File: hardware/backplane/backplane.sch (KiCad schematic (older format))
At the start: 88 parts, among them J1 C96ABC, J10 Conn_Coaxial_Power, J2 C96ABC, J3 C96ABC, J4 C96ABC, J5 C96ABC, J6 C96ABC, J7 C96ABC, J8 C96ABC, J9 C96ABC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

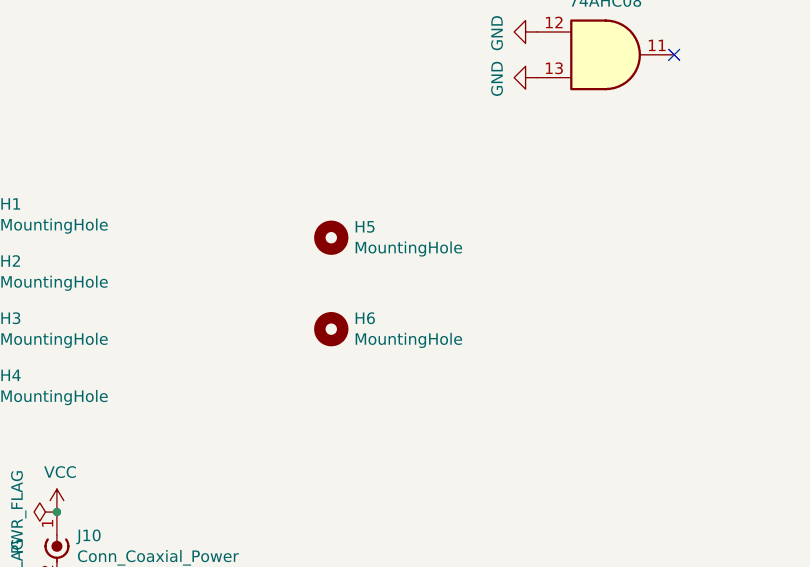
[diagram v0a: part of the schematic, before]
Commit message: backplane: reduce mounting hardware used
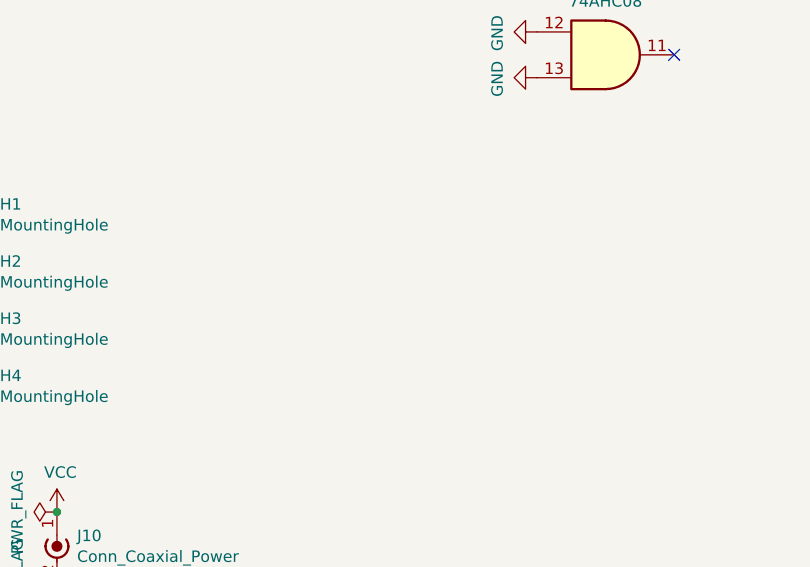
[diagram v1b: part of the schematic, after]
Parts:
- removed H5, H6: MountingHole, rails:7mm, symbol Mechanical:MountingHole
- H1, H2, H3, H4: footprint rails:8mm -> rails:m5-close
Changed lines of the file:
@@
 F 0 "H4" H 12250 5546 50  0000 L CNN
 F 1 "MountingHole" H 12250 5455 50  0000 L CNN
-F 2 "rails:8mm" H 12150 5500 50  0001 C CNN
+F 2 "rails:m5-close" H 12150 5500 50  0001 C CNN
 F 3 "~" H 12150 5500 50  0001 C CNN
 	1    12150 5500
@@
 F 0 "H3" H 12250 5296 50  0000 L CNN
 F 1 "MountingHole" H 12250 5205 50  0000 L CNN
-F 2 "rails:8mm" H 12150 5250 50  0001 C CNN
+F 2 "rails:m5-close" H 12150 5250 50  0001 C CNN
 F 3 "~" H 12150 5250 50  0001 C CNN
 	1    12150 5250
@@
 F 0 "H2" H 12250 5046 50  0000 L CNN
 F 1 "MountingHole" H 12250 4955 50  0000 L CNN
-F 2 "rails:8mm" H 12150 5000 50  0001 C CNN
+F 2 "rails:m5-close" H 12150 5000 50  0001 C CNN
 F 3 "~" H 12150 5000 50  0001 C CNN
 	1    12150 5000
@@
 F 0 "H1" H 12250 4796 50  0000 L CNN
 F 1 "MountingHole" H 12250 4705 50  0000 L CNN
-F 2 "rails:8mm" H 12150 4750 50  0001 C CNN
+F 2 "rails:m5-close" H 12150 4750 50  0001 C CNN
 F 3 "~" H 12150 4750 50  0001 C CNN
 	1    12150 4750
@@
 	-650 -2650 -700 -2650
 $Comp
-L Mechanical:MountingHole H5
-U 1 1 A242A775
-P 13700 4850
-F 0 "H5" H 13800 4896 50  0000 L CNN
-F 1 "MountingHole" H 13800 4805 50  0000 L CNN
-F 2 "rails:7mm" H 13700 4850 50  0001 C CNN
-F 3 "~" H 13700 4850 50  0001 C CNN
-	1    13700 4850
-	1    0    0    -1
-$EndComp
-$Comp
-L Mechanical:MountingHole H6
-U 1 1 A2589AFB
-P 13700 5250
-F 0 "H6" H 13800 5296 50  0000 L CNN
-F 1 "MountingHole" H 13800 5205 50  0000 L CNN
-F 2 "rails:7mm" H 13700 5250 50  0001 C CNN
-F 3 "~" H 13700 5250 50  0001 C CNN
-	1    13700 5250
-	1    0    0    -1
-$EndComp
-$Comp
 L Device:D_Schottky_x2_KCom_AAK D3

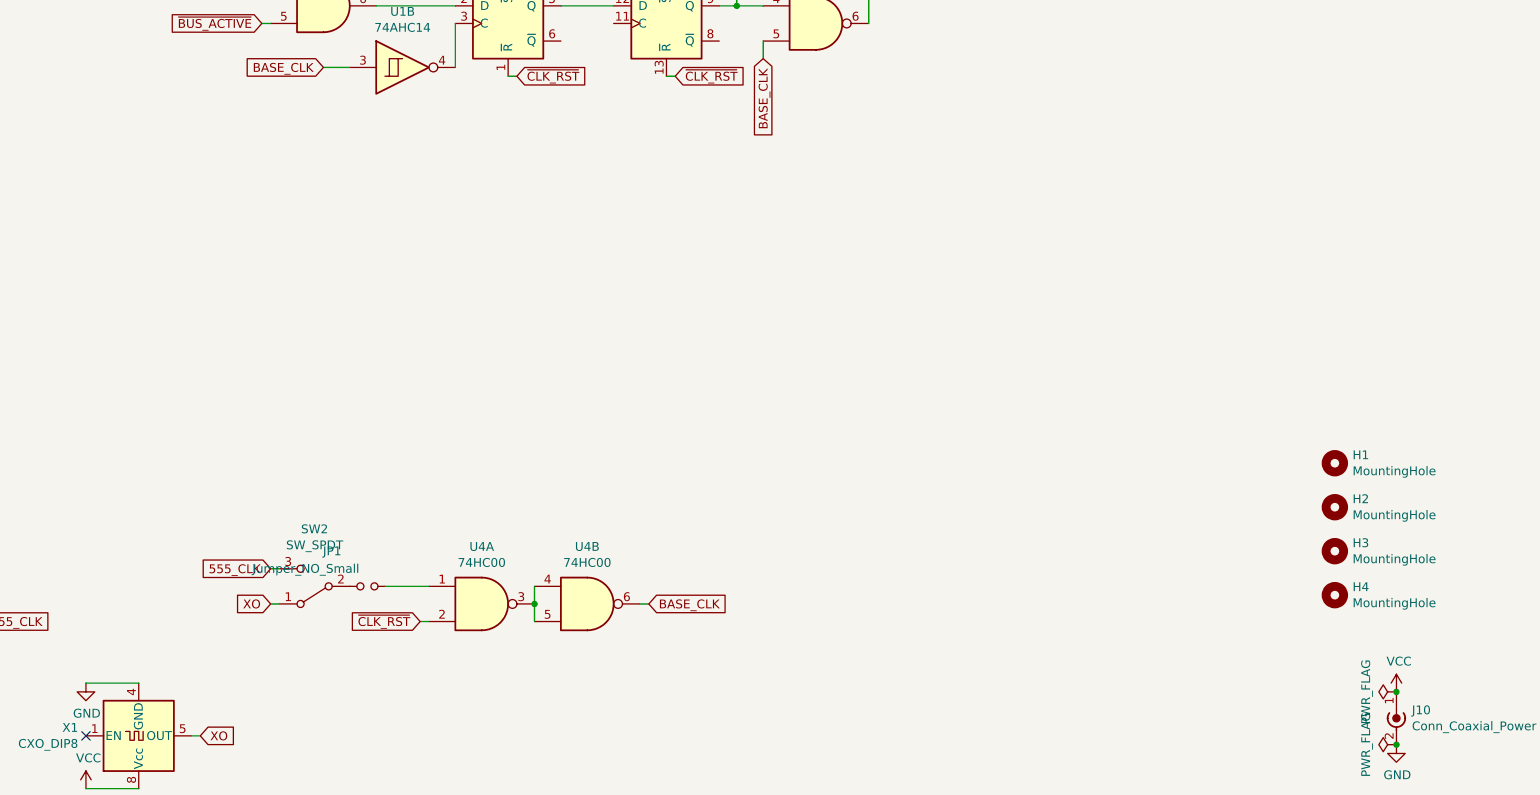
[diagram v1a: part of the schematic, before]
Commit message: backplane: add soft power on/off circuit to backplane
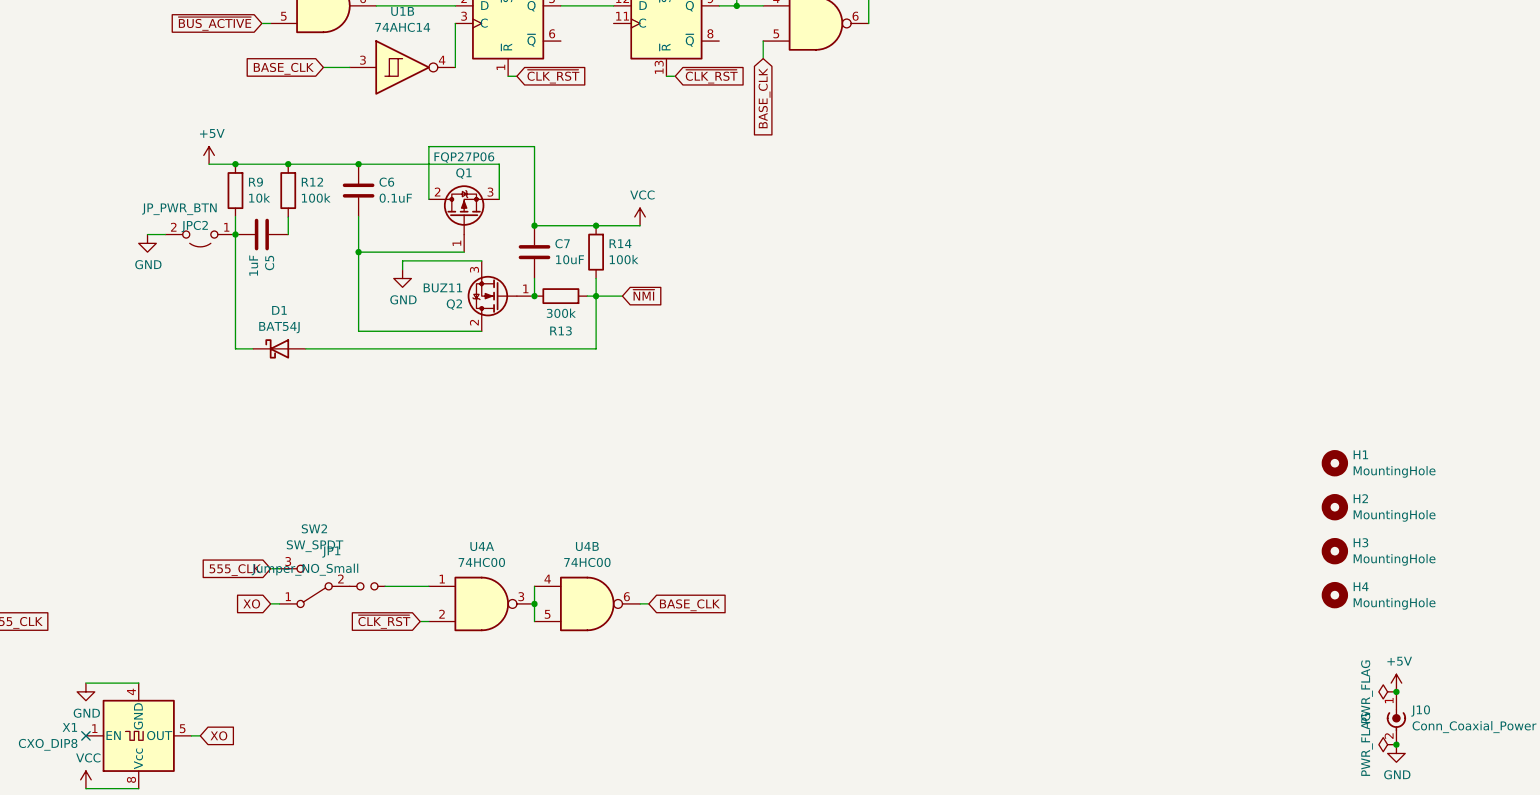
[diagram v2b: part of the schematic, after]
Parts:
- added C5: 1uF, Capacitor_THT:C_Axial_L5.1mm_D3.1mm_P7.50mm_Horizontal, symbol Device:C
- added C6: 0.1uF, Capacitor_THT:C_Disc_D4.7mm_W2.5mm_P5.00mm, symbol Device:C
- added C7: 10uF, Capacitor_THT:C_Axial_L5.1mm_D3.1mm_P7.50mm_Horizontal, symbol Device:C
- added D1: BAT54J, Diode_THT:D_A-405_P7.62mm_Horizontal, symbol Diode:BAT54J
- added JPC2: JP_PWR_BTN, Connector_PinHeader_2.54mm:PinHeader_1x02_P2.54mm_Vertical, symbol Jumper:Jumper_2_Open
- added Q1: FQP27P06, Package_TO_SOT_THT:TO-220-3_Horizontal_TabDown, symbol Transistor_FET:FQP27P06
- added Q2: BUZ11, Package_TO_SOT_THT:TO-220-3_Horizontal_TabDown, symbol Transistor_FET:BUZ11
- added R12, R14: 100k, Resistor_THT:R_Axial_DIN0207_L6.3mm_D2.5mm_P7.62mm_Horizontal, symbol Device:R
- added R13: 300k, Resistor_THT:R_Axial_DIN0207_L6.3mm_D2.5mm_P7.62mm_Horizontal, symbol Device:R
- added R9: 10k, Resistor_THT:R_Axial_DIN0207_L6.3mm_D2.5mm_P7.62mm_Horizontal, symbol Device:R
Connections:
- net A30: now also D1.2 (A), R13.2, R14.1
- net GND: now also JPC2.2 (B), Q2.3 (S)
- net VCC: now also C7.1, Q1.2 (D), R14.2; no longer J10.1 (In)
- new net: C6.2, Q1.1 (G), Q2.2 (D)
- new net: C7.2, Q2.1 (G), R13.1
- new net: C5.2, D1.1 (K), JPC2.1 (A), R9.1
- new net: C5.1, R12.1
- new net +5V: C6.1, J10.1 (In), Q1.3 (S), R12.2, R9.2
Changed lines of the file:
@@
 $EndDescr
 $Comp
-L power:VCC #PWR055
-U 1 1 60477C9A
-P 12500 6050
-F 0 "#PWR055" H 12500 5900 50  0001 C CNN
-F 1 "VCC" H 12515 6223 50  0000 C CNN
-F 2 "" H 12500 6050 50  0001 C CNN
-F 3 "" H 12500 6050 50  0001 C CNN
-	1    12500 6050
-	1    0    0    -1
-$EndComp
-$Comp
 L power:GND #PWR056
 U 1 1 60478083
@@
 $EndComp
 Connection ~ 12500 6350
-Connection ~ 12500 6050
 $Comp
 L Connector:TestPoint TP1
@@
 	1    0    0    -1
 $EndComp
+$Comp
+L Transistor_FET:BUZ11 Q2
+U 1 1 610FD02B
+P 7400 3800
+F 0 "Q2" H 7605 3846 50  0000 L CNN
+F 1 "BUZ11" H 7605 3755 50  0000 L CNN
+F 2 "Package_TO_SOT_THT:TO-220-3_Horizontal_TabDown" H 7650 3725 50  0001 L CIN
+F 3 "https://media.digikey.com/pdf/Data%20Sheets/Fairchild%20PDFs/BUZ11.pdf" H 7400 3800 50  0001 L CNN
+	1    7400 3800
+	-1   0    0    1
+$EndComp
+$Comp
+L power:GND #PWR0103
+U 1 1 61589CAB
+P 6850 3650
+F 0 "#PWR0103" H 6850 3400 50  0001 C CNN
+F 1 "GND" H 6855 3477 50  0000 C CNN
+F 2 "" H 6850 3650 50  0001 C CNN
+F 3 "" H 6850 3650 50  0001 C CNN
+	1    6850 3650
+	1    0    0    -1
+$EndComp
+Wire Wire Line
+	6850 3650 6850 3600
+Wire Wire Line
+	6850 3600 7300 3600
+$Comp
+L Device:R R13
+U 1 1 61710642
+P 7750 3800
+F 0 "R13" V 7550 3800 50  0000 C CNN
+F 1 "300k" V 7650 3800 50  0000 C CNN
+F 2 "Resistor_THT:R_Axial_DIN0207_L6.3mm_D2.5mm_P7.62mm_Horizontal" V 7680 3800 50  0001 C CNN
+F 3 "~" H 7750 3800 50  0001 C CNN
+	1    7750 3800
+	0    -1   -1   0
+$EndComp
+$Comp
+L Device:R R14
+U 1 1 61899D83
+P 7950 3550
+F 0 "R14" H 7880 3504 50  0000 R CNN
+F 1 "100k" H 7880 3595 50  0000 R CNN
+F 2 "Resistor_THT:R_Axial_DIN0207_L6.3mm_D2.5mm_P7.62mm_Horizontal" V 7880 3550 50  0001 C CNN
+F 3 "~" H 7950 3550 50  0001 C CNN
+	1    7950 3550
+	-1   0    0    1
+$EndComp
+Wire Wire Line
+	7950 3700 7950 3800
+$Comp
+L Device:C C7
+U 1 1 61A1E32F
+P 7600 3550
+F 0 "C7" H 7715 3596 50  0000 L CNN
+F 1 "10uF" H 7715 3505 50  0000 L CNN
+F 2 "Capacitor_THT:C_Axial_L5.1mm_D3.1mm_P7.50mm_Horizontal" H 7638 3400 50  0001 C CNN
+F 3 "~" H 7600 3550 50  0001 C CNN
+	1    7600 3550
+	1    0    0    -1
+$EndComp
+Wire Wire Line
+	7600 3800 7600 3700
+Wire Wire Line
+	7950 3800 7900 3800
+Wire Wire Line
+	7600 3400 7950 3400
+Connection ~ 7600 3400
+$Comp
+L power:+5V #PWR0108
+U 1 1 6295B29C
+P 12500 6050
+F 0 "#PWR0108" H 12500 5900 50  0001 C CNN
+F 1 "+5V" H 12515 6223 50  0000 C CNN
+F 2 "" H 12500 6050 50  0001 C CNN
+F 3 "" H 12500 6050 50  0001 C CNN
+	1    12500 6050
+	1    0    0    -1
+$EndComp
+Connection ~ 12500 6050
+$Comp
+L power:VCC #PWR055
+U 1 1 60477C9A
+P 8200 3400
+F 0 "#PWR055" H 8200 3250 50  0001 C CNN
+F 1 "VCC" H 8215 3573 50  0000 C CNN
+F 2 "" H 8200 3400 50  0001 C CNN
+F 3 "" H 8200 3400 50  0001 C CNN
+	1    8200 3400
+	1    0    0    -1
+$EndComp
+Wire Wire Line
+	7950 3400 8200 3400
+Connection ~ 7950 3400
+$Comp
+L power:+5V #PWR0109
+U 1 1 63284480
+P 5750 3050
+F 0 "#PWR0109" H 5750 2900 50  0001 C CNN
+F 1 "+5V" H 5765 3223 50  0000 C CNN
+F 2 "" H 5750 3050 50  0001 C CNN
+F 3 "" H 5750 3050 50  0001 C CNN
+	1    5750 3050
+	1    0    0    -1
+$EndComp
+Wire Wire Line
+	5750 3050 5900 3050
+$Comp
+L Device:R R9
+U 1 1 635960F7
+P 5900 3200
+F 0 "R9" H 5830 3154 50  0000 R CNN
+F 1 "10k" H 5830 3245 50  0000 R CNN
+F 2 "Resistor_THT:R_Axial_DIN0207_L6.3mm_D2.5mm_P7.62mm_Horizontal" V 5830 3200 50  0001 C CNN
+F 3 "~" H 5900 3200 50  0001 C CNN
+	1    5900 3200
+	-1   0    0    1
+$EndComp
+Connection ~ 5900 3050
+Wire Wire Line
+	5900 3050 6200 3050
+$Comp
+L Device:R R12
+U 1 1 6359666D
+P 6200 3200
+F 0 "R12" H 6130 3154 50  0000 R CNN
+F 1 "100k" H 6130 3245 50  0000 R CNN
+F 2 "Resistor_THT:R_Axial_DIN0207_L6.3mm_D2.5mm_P7.62mm_Horizontal" V 6130 3200 50  0001 C CNN
+F 3 "~" H 6200 3200 50  0001 C CNN
+	1    6200 3200
+	-1   0    0    1
+$EndComp
+Connection ~ 6200 3050
+Wire Wire Line
+	6200 3050 6600 3050
+$Comp
+L Device:C C6
+U 1 1 6359692F
+P 6600 3200
+F 0 "C6" H 6715 3246 50  0000 L CNN
+F 1 "0.1uF" H 6715 3155 50  0000 L CNN
+F 2 "Capacitor_THT:C_Disc_D4.7mm_W2.5mm_P5.00mm" H 6638 3050 50  0001 C CNN
+F 3 "~" H 6600 3200 50  0001 C CNN
+	1    6600 3200
+	1    0    0    -1
+$EndComp
+Connection ~ 6600 3050
+$Comp
+L Transistor_FET:FQP27P06 Q1
+U 1 1 60AF6494
+P 7200 3350
+F 0 "Q1" V 7449 3350 50  0000 C CNN
+F 1 "FQP27P06" V 7540 3350 50  0000 C CNN
+F 2 "Package_TO_SOT_THT:TO-220-3_Horizontal_TabDown" H 7400 3275 50  0001 L CIN
+F 3 "https://www.onsemi.com/pub/Collateral/FQP27P06-D.PDF" H 7200 3350 50  0001 L CNN
+	1    7200 3350
+	0    -1   -1   0
+$EndComp
+Wire Wire Line
+	7400 3050 7400 3250
+Wire Wire Line
+	6600 3050 7400 3050
+Wire Wire Line
+	7000 3250 7000 2950
+Wire Wire Line
+	7000 2950 7600 2950
+Wire Wire Line
+	7600 2950 7600 3400
+Wire Wire Line
+	6200 3350 6200 3450
+Wire Wire Line
+	5900 3350 5900 3450
+$Comp
+L Device:C C5
+U 1 1 63D536BB
+P 6050 3450
+F 0 "C5" H 6165 3496 50  0000 L CNN
+F 1 "1uF" H 6165 3405 50  0000 L CNN
+F 2 "Capacitor_THT:C_Axial_L5.1mm_D3.1mm_P7.50mm_Horizontal" H 6088 3300 50  0001 C CNN
+F 3 "~" H 6050 3450 50  0001 C CNN
+	1    6050 3450
+	0    1    1    0
+$EndComp
+Wire Wire Line
+	6600 4000 6600 3550
+Wire Wire Line
+	7200 3550 6600 3550
+Connection ~ 6600 3550
+Wire Wire Line
+	6600 3550 6600 3350
+Wire Wire Line
+	7300 4000 6600 4000
+Connection ~ 7600 3800
+$Comp
+L Diode:BAT54J D1
+U 1 1 6549C471
+P 6150 4100
+F 0 "D1" H 6150 4317 50  0000 C CNN
+F 1 "BAT54J" H 6150 4226 50  0000 C CNN
+F 2 "Diode_THT:D_A-405_P7.62mm_Horizontal" H 6150 3925 50  0001 C CNN
+F 3 "https://assets.nexperia.com/documents/data-sheet/BAT54J.pdf" H 6150 4100 50  0001 C CNN
+	1    6150 4100
+	1    0    0    -1
+$EndComp
+Wire Wire Line
+	7950 3800 7950 4100
+Wire Wire Line
+	7950 4100 6300 4100
+Connection ~ 7950 3800
+Wire Wire Line
+	6000 4100 5900 4100
+Wire Wire Line
+	5900 4100 5900 3450
+Connection ~ 5900 3450
+$Comp
+L Jumper:Jumper_2_Open JPC2
+U 1 1 65ADC663
+P 5700 3450
+F 0 "JPC2" H 5650 3400 50  0000 L CNN
+F 1 "JP_PWR_BTN" H 5600 3300 50  0000 L CNN
+F 2 "Connector_PinHeader_2.54mm:PinHeader_1x02_P2.54mm_Vertical" H 5700 3450 50  0001 C CNN
+F 3 "~" H 5700 3450 50  0001 C CNN
+	1    5700 3450
+	-1   0    0    1
+$EndComp
+$Comp
+L power:GND #gnd0115
+U 1 1 65ADD10B
+P 5400 3450
+F 0 "#gnd0115" H 5400 3200 50  0001 C CNN
+F 1 "GND" H 5405 3277 50  0000 C CNN
+F 2 "" H 5400 3450 50  0001 C CNN
+F 3 "" H 5400 3450 50  0001 C CNN
+	1    5400 3450
+	1    0    0    -1
+$EndComp
+Wire Wire Line
+	5500 3450 5400 3450
+Text GLabel 8100 3800 2    50   Input ~ 0
+~NMI~
+Wire Wire Line
+	8100 3800 7950 3800
 $EndSCHEMATC

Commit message: backplane: minor improvements
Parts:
- removed D3: D_Schottky_x2_KCom_AAK, Package_TO_SOT_SMD:SOT-23_Handsoldering, symbol Device:D_Schottky_x2_KCom_AAK
- added C8: CP, Capacitor_THT:CP_Radial_D10.0mm_P5.00mm, symbol Device:CP
- added D2, D4: LED, LED_THT:LED_D3.0mm, symbol Device:LED
- added D3, D5: BAT54J, Diode_THT:D_A-405_P7.62mm_Horizontal, symbol Diode:BAT54J
- added R15, R16: 1k, Resistor_THT:R_Axial_DIN0207_L6.3mm_D2.5mm_P7.62mm_Horizontal, symbol Device:R
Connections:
- net +5V: now also C8.1, D4.2 (A)
- net GND: now also C8.2, R15.1, R16.1
- net VCC: now also D2.2 (A)
- net ~RST_HDR~: now also D3.1 (K), D5.1 (K)
- net at CR1.1, R2.2, U1.5: now also D3.2 (A)
- net at CR2.1, R3.2, U1.13: now also D5.2 (A)
- new net: D2.1 (K), R15.2
- new net: D4.1 (K), R16.2
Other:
- moved on the sheet: C5, C6, C7, CBU1, CBU10, CBU2, CBU3, CBU4, CBU5, CBU6, CBU7, CBU8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

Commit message: start adding reverse voltage protection
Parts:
- removed JPC1: JP_RST, Connector_PinHeader_2.54mm:PinHeader_1x02_P2.54mm_Vertical, symbol Jumper:Jumper_2_Open
- removed JPC2: JP_PWR_BTN, Connector_PinHeader_2.54mm:PinHeader_1x02_P2.54mm_Vertical, symbol Jumper:Jumper_2_Open
- added D?: D_Zener, Diode_THT:D_A-405_P7.62mm_Horizontal, symbol Device:D_Zener
- added F?: Fuse, symbol Device:Fuse
- added Q?: FQP27P06, Package_TO_SOT_THT:TO-220-3_Horizontal_TabDown, symbol Transistor_FET:FQP27P06
- added R?: 100k, Resistor_THT:R_Axial_DIN0207_L6.3mm_D2.5mm_P7.62mm_Horizontal, symbol Device:R
- added SW4, SW5: SW_Push, Connector_PinHeader_2.54mm:PinHeader_1x02_P2.54mm_Vertical, symbol Switch:SW_Push
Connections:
- net +5V: now also D?.1 (K), Q?.3 (S); no longer J10.1 (In)
- net GND: now also R?.1, SW4.1, SW5.2
- net ~RST_HDR~: now also SW4.2
- net at C5.2, D1.1 (K), R9.1: now also SW5.1
- new net: D?.2 (A), Q?.1 (G), R?.2
- new net: F?.2, J10.1 (In)
- new net +VDC: F?.1, Q?.2 (D)
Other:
- note added: "Reverse voltage protection"
- note added: "Soft power"
- note added: "TODO: values for zener and resistor"
- moved on the sheet: C5, C6, C7, C8, CBU1, CBU10, CBU2, CBU3, CBU4, CBU5, CBU6, CBU7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
